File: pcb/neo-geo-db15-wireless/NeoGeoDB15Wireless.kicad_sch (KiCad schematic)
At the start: 3 parts, among them J1 DB15_Female_MountingHoles, U1 RP2040-Zero, U2 NRF24L01_Breakout

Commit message: PCB schematic
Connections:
- net GND: now reaches U1.23 (GND), U2.1 (GND)
- net GND: now also J1.1
- net at U1.20 (GP29): no longer U2.3 (CE)
- net CS: now reaches U2.4 (~{CSN})
- net CS: now also U1.14 (GP13)
- net SCK: now reaches U2.5 (SCK)
- net SCK: now also U1.15 (GP14)
- net MOSI: now reaches U2.6 (MOSI)
- net MOSI: now also U1.16 (GP15)
- net MISO: now reaches U2.7 (MISO)
- net MISO: now also U1.13 (GP12)
- net at U1.19 (GP28): no longer U2.8 (IRQ)
- net DU: now reaches U1.1 (GP0)
- net DU: now also J1.15 (P15)
- net SEL: now reaches U1.10 (GP9)
- net SEL: now also J1.3
- net CE: now reaches U1.17 (GP26)
- net CE: now also U2.3 (CE)
- net IRQ: now reaches U1.18 (GP27)
- net IRQ: now also U2.8 (IRQ)
- net DD: now reaches U1.2 (GP1)
- net DD: now also J1.7
- net VCC: now reaches U1.22 (5V)
- net VCC: now also J1.8
- net DL: now reaches U1.3 (GP2)
- net DL: now also J1.14 (P14)
- net DR: now reaches U1.4 (GP3)
- net DR: now also J1.6
- net BA: now reaches U1.5 (GP4)
- net BA: now also J1.13 (P13)
- net BB: now reaches U1.6 (GP5)
- net BB: now also J1.5
- net BC: now reaches U1.7 (GP6)
- net BC: now also J1.12 (P12)
- net BD: now reaches U1.8 (GP7)
- net BD: now also J1.4
- net STA: now reaches U1.9 (GP8)
- net STA: now also J1.11 (P111)
- no-connect marks 0 -> 8
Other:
- moved on the sheet: J1
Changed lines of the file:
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@@
 (kicad_sch (version 20211123) (generator eeschema)
   (paper "A4")
-  (wire (pts (xy 115.57 92.71) (xy 115.57 83.82))
-    (stroke (width 0) (type default) (color 0 0 0 0))
-  )
-  (wire (pts (xy 153.67 76.2) (xy 130.81 58.42))
-    (stroke (width 0) (type default) (color 0 0 0 0))
-  )
-  (wire (pts (xy 166.37 83.82) (xy 166.37 92.71))
-    (stroke (width 0) (type default) (color 0 0 0 0))
-  )
-  (wire (pts (xy 153.67 73.66) (xy 130.81 55.88))
-    (stroke (width 0) (type default) (color 0 0 0 0))
-  )
+  (no_connect (at 130.81 76.2))
+  (no_connect (at 130.81 78.74))
+  (no_connect (at 130.81 55.88))
+  (no_connect (at 130.81 58.42))
+  (no_connect (at 152.4 24.13))
+  (no_connect (at 149.86 24.13))
+  (no_connect (at 154.94 24.13))
+  (no_connect (at 116.84 31.75))
   (wire (pts (xy 116.84 49.53) (xy 166.37 49.53))
     (stroke (width 0) (type default) (color 0 0 0 0))
@@
     (stroke (width 0) (type default) (color 0 0 0 0))
   )
-  (wire (pts (xy 166.37 92.71) (xy 115.57 92.71))
-    (stroke (width 0) (type default) (color 0 0 0 0))
+  (label "BD" (at 142.24 24.13 90)
+    (effects (font (size 1.27 1.27)) (justify left bottom))
+  )
+  (label "DR" (at 132.08 24.13 90)
+    (effects (font (size 1.27 1.27)) (justify left bottom))
+  )
+  (label "CS" (at 130.81 71.12 0)
+    (effects (font (size 1.27 1.27)) (justify left bottom))
+  )
+  (label "GND" (at 115.57 83.82 270)
+    (effects (font (size 1.27 1.27)) (justify right bottom))
+  )
+  (label "BC" (at 139.7 24.13 90)
+    (effects (font (size 1.27 1.27)) (justify left bottom))
+  )
+  (label "BB" (at 101.6 68.58 180)
+    (effects (font (size 1.27 1.27)) (justify right bottom))
+  )
+  (label "BD" (at 101.6 73.66 180)
+    (effects (font (size 1.27 1.27)) (justify right bottom))
+  )
+  (label "VCC" (at 121.92 24.13 90)
+    (effects (font (size 1.27 1.27)) (justify left bottom))
+  )
+  (label "SCK" (at 130.81 68.58 0)
+    (effects (font (size 1.27 1.27)) (justify left bottom))
+  )
+  (label "IRQ" (at 153.67 76.2 180)
+    (effects (font (size 1.27 1.27)) (justify right bottom))
+  )
+  (label "VCC" (at 114.3 49.53 90)
+    (effects (font (size 1.27 1.27)) (justify left bottom))
+  )
+  (label "DU" (at 101.6 55.88 180)
+    (effects (font (size 1.27 1.27)) (justify right bottom))
+  )
+  (label "DR" (at 101.6 63.5 180)
+    (effects (font (size 1.27 1.27)) (justify right bottom))
+  )
+  (label "CE" (at 153.67 73.66 180)
+    (effects (font (size 1.27 1.27)) (justify right bottom))
+  )
+  (label "STA" (at 101.6 76.2 180)
+    (effects (font (size 1.27 1.27)) (justify right bottom))
+  )
+  (label "DD" (at 127 24.13 90)
+    (effects (font (size 1.27 1.27)) (justify left bottom))
+  )
+  (label "MISO" (at 130.81 73.66 0)
+    (effects (font (size 1.27 1.27)) (justify left bottom))
+  )
+  (label "CE" (at 130.81 63.5 0)
+    (effects (font (size 1.27 1.27)) (justify left bottom))
+  )
+  (label "CS" (at 153.67 68.58 180)
+    (effects (font (size 1.27 1.27)) (justify right bottom))
+  )
+  (label "GND" (at 157.48 24.13 90)
+    (effects (font (size 1.27 1.27)) (justify left bottom))
+  )
+  (label "BC" (at 101.6 71.12 180)
+    (effects (font (size 1.27 1.27)) (justify right bottom))
+  )
+  (label "BA" (at 101.6 66.04 180)
+    (effects (font (size 1.27 1.27)) (justify right bottom))
+  )
+  (label "SCK" (at 153.67 66.04 180)
+    (effects (font (size 1.27 1.27)) (justify right bottom))
+  )
+  (label "BB" (at 137.16 24.13 90)
+    (effects (font (size 1.27 1.27)) (justify left bottom))
+  )
+  (label "MOSI" (at 130.81 66.04 0)
+    (effects (font (size 1.27 1.27)) (justify left bottom))
+  )
+  (label "MISO" (at 153.67 63.5 180)
+    (effects (font (size 1.27 1.27)) (justify right bottom))
+  )
+  (label "BA" (at 134.62 24.13 90)
+    (effects (font (size 1.27 1.27)) (justify left bottom))
+  )
+  (label "DU" (at 124.46 24.13 90)
+    (effects (font (size 1.27 1.27)) (justify left bottom))
+  )
+  (label "STA" (at 144.78 24.13 90)
+    (effects (font (size 1.27 1.27)) (justify left bottom))
+  )
+  (label "DD" (at 101.6 58.42 180)
+    (effects (font (size 1.27 1.27)) (justify right bottom))
+  )
+  (label "MOSI" (at 153.67 60.96 180)
+    (effects (font (size 1.27 1.27)) (justify right bottom))
+  )
+  (label "DL" (at 101.6 60.96 180)
+    (effects (font (size 1.27 1.27)) (justify right bottom))
+  )
+  (label "SEL" (at 101.6 78.74 180)
+    (effects (font (size 1.27 1.27)) (justify right bottom))
+  )
+  (label "DL" (at 129.54 24.13 90)
+    (effects (font (size 1.27 1.27)) (justify left bottom))
+  )
+  (label "IRQ" (at 130.81 60.96 0)
+    (effects (font (size 1.27 1.27)) (justify left bottom))
+  )
+  (label "GND" (at 166.37 83.82 270)
+    (effects (font (size 1.27 1.27)) (justify right bottom))
+  )
+  (label "SEL" (at 147.32 24.13 90)
+    (effects (font (size 1.27 1.27)) (justify left bottom))
   )
   (symbol (lib_id "RF:NRF24L01_Breakout") (at 166.37 68.58 0) (unit 1)
@@
     (pin "9")
   )
-  (symbol (lib_id "Connector:DB15_Female_MountingHoles") (at 139.7 31.75 90) (unit 1)
+  (symbol (lib_id "Connector:DB15_Female_MountingHoles") (at 139.7 31.75 270) (unit 1)
     (in_bom yes) (on_board yes) (fields_autoplaced)
-    (property "Reference" "J1" (id 0) (at 139.7 22.86 90))
-    (property "Value" "DB15_Female_MountingHoles" (id 1) (at 139.7 25.4 90))
+    (property "Reference" "J1" (id 0) (at 139.7 38.1 90))
+    (property "Value" "DB15_Female_MountingHoles" (id 1) (at 139.7 40.64 90))
     (property "Footprint" "DB15:TE_Connectivity-5747845-5-0-0-MFG" (id 2) (at 139.7 31.75 0)
       (effects (font (size 1.27 1.27)) hide)

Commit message: Making the right size
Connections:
- net 3V3: now reaches U1.21 (3V3), U2.2 (VCC)
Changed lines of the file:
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@@
   (no_connect (at 154.94 24.13))
   (no_connect (at 116.84 31.75))
-  (wire (pts (xy 116.84 49.53) (xy 166.37 49.53))
-    (stroke (width 0) (type default) (color 0 0 0 0))
-  )
-  (wire (pts (xy 166.37 49.53) (xy 166.37 53.34))
-    (stroke (width 0) (type default) (color 0 0 0 0))
-  )
   (label "BD" (at 142.24 24.13 90)
     (effects (font (size 1.27 1.27)) (justify left bottom))
@@
   )
   (label "BC" (at 139.7 24.13 90)
+    (effects (font (size 1.27 1.27)) (justify left bottom))
+  )
+  (label "3V3" (at 116.84 49.53 90)
     (effects (font (size 1.27 1.27)) (justify left bottom))
   )
@@
     (effects (font (size 1.27 1.27)) (justify right bottom))
   )
+  (label "3V3" (at 166.37 53.34 90)
+    (effects (font (size 1.27 1.27)) (justify left bottom))
+  )
   (label "VCC" (at 114.3 49.53 90)

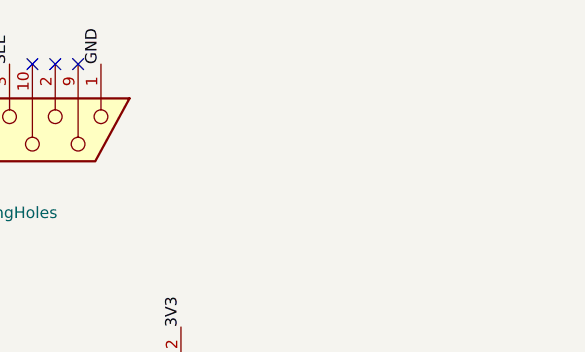
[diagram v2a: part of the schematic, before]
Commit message: Adds decoupling caps
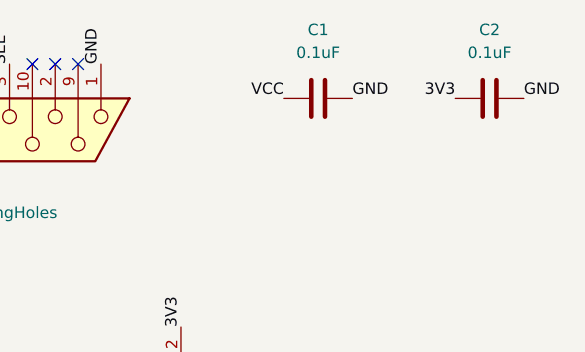
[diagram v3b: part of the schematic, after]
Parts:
- added C1, C2: 0.1uF, Capacitor_SMD:C_0603_1608Metric_Pad1.08x0.95mm_HandSolder, symbol Device:C
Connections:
- net 3V3: now also C2.1
- net GND: now also C1.2, C2.2
- net VCC: now also C1.1
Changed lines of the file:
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@@
     (effects (font (size 1.27 1.27)) (justify left bottom))
+  )
+  (label "3V3" (at 196.85 27.94 180)
+    (effects (font (size 1.27 1.27)) (justify right bottom))
   )
   (label "MISO" (at 130.81 73.66 0)
@@
     (effects (font (size 1.27 1.27)) (justify right bottom))
   )
+  (label "VCC" (at 177.8 27.94 180)
+    (effects (font (size 1.27 1.27)) (justify right bottom))
+  )
   (label "BA" (at 134.62 24.13 90)
     (effects (font (size 1.27 1.27)) (justify left bottom))
@@
     (effects (font (size 1.27 1.27)) (justify left bottom))
   )
+  (label "GND" (at 204.47 27.94 0)
+    (effects (font (size 1.27 1.27)) (justify left bottom))
+  )
   (label "STA" (at 144.78 24.13 90)
+    (effects (font (size 1.27 1.27)) (justify left bottom))
+  )
+  (label "GND" (at 185.42 27.94 0)
     (effects (font (size 1.27 1.27)) (justify left bottom))
   )
@@
     (pin "7")
     (pin "8")
+  )
+  (symbol (lib_id "Device:C") (at 181.61 27.94 90) (unit 1)
+    (in_bom yes) (on_board yes) (fields_autoplaced)
+    (property "Reference" "C1" (id 0) (at 181.61 20.32 90))
+    (property "Value" "0.1uF" (id 1) (at 181.61 22.86 90))
+    (property "Footprint" "Capacitor_SMD:C_0603_1608Metric_Pad1.08x0.95mm_HandSolder" (id 2) (at 185.42 26.9748 0)
+      (effects (font (size 1.27 1.27)) hide)
+    )
+    (property "Datasheet" "~" (id 3) (at 181.61 27.94 0)
+      (effects (font (size 1.27 1.27)) hide)
+    )
+    (pin "1")
+    (pin "2")
   )
   (symbol (lib_id "RP2040Zero:RP2040-Zero") (at 115.57 66.04 0) (unit 1)
@@
     (pin "9")
   )
+  (symbol (lib_id "Device:C") (at 200.66 27.94 90) (unit 1)
+    (in_bom yes) (on_board yes) (fields_autoplaced)
+    (property "Reference" "C2" (id 0) (at 200.66 20.32 90))
+    (property "Value" "0.1uF" (id 1) (at 200.66 22.86 90))
+    (property "Footprint" "Capacitor_SMD:C_0603_1608Metric_Pad1.08x0.95mm_HandSolder" (id 2) (at 204.47 26.9748 0)
+      (effects (font (size 1.27 1.27)) hide)
+    )
+    (property "Datasheet" "~" (id 3) (at 200.66 27.94 0)
+      (effects (font (size 1.27 1.27)) hide)
+    )
+    (pin "1")
+    (pin "2")
+  )
   (sheet_instances
     (path "/" (page "1"))
   )
   (symbol_instances
+    (path "/5600fa70-7237-419a-a1e7-e59e3f85f285"
+      (reference "C1") (unit 1) (value "0.1uF") (footprint "Capacitor_SMD:C_0603_1608Metric_Pad1.08x0.95mm_HandSolder")
+    )
+    (path "/efed16f8-8695-4c2e-90ae-063653f0ab84"
+      (reference "C2") (unit 1) (value "0.1uF") (footprint "Capacitor_SMD:C_0603_1608Metric_Pad1.08x0.95mm_HandSolder")
+    )
     (path "/dad04a51-3cbf-4f9b-b9b9-52635f5ef12c"
       (reference "J1") (unit 1) (value "DB15_Female_MountingHoles") (footprint "DB15:TE_Connectivity-5747845-5-0-0-MFG")

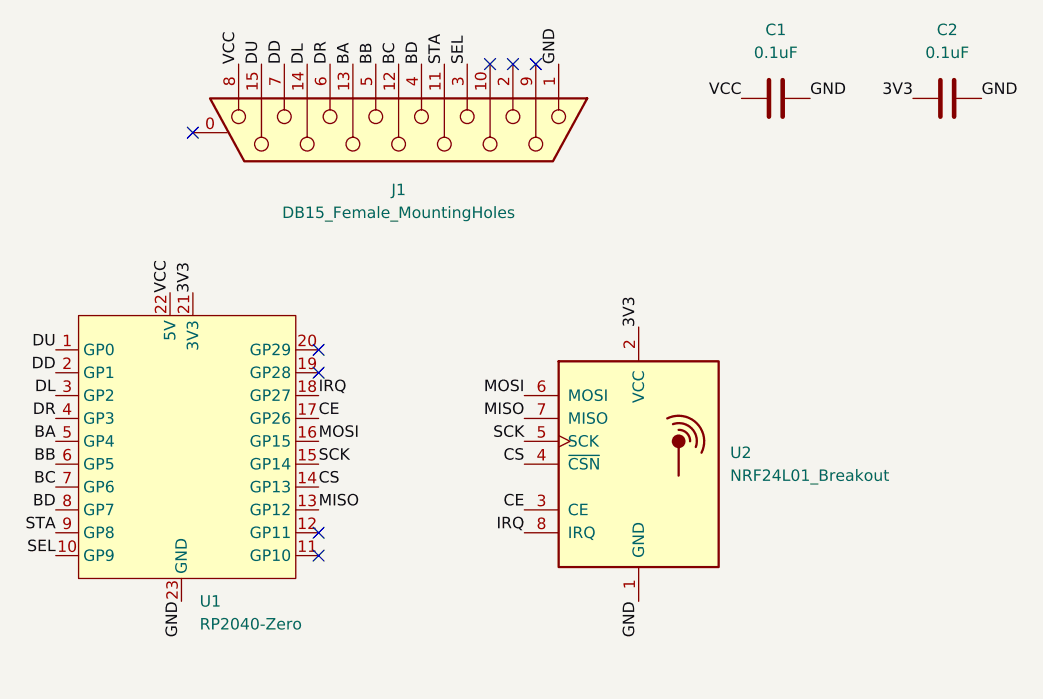
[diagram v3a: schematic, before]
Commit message: Fixes errors in PCB, incorrect pin numbering on RP2040, unconnected grounds, ground mounting points, some vias to increase ground plane flood
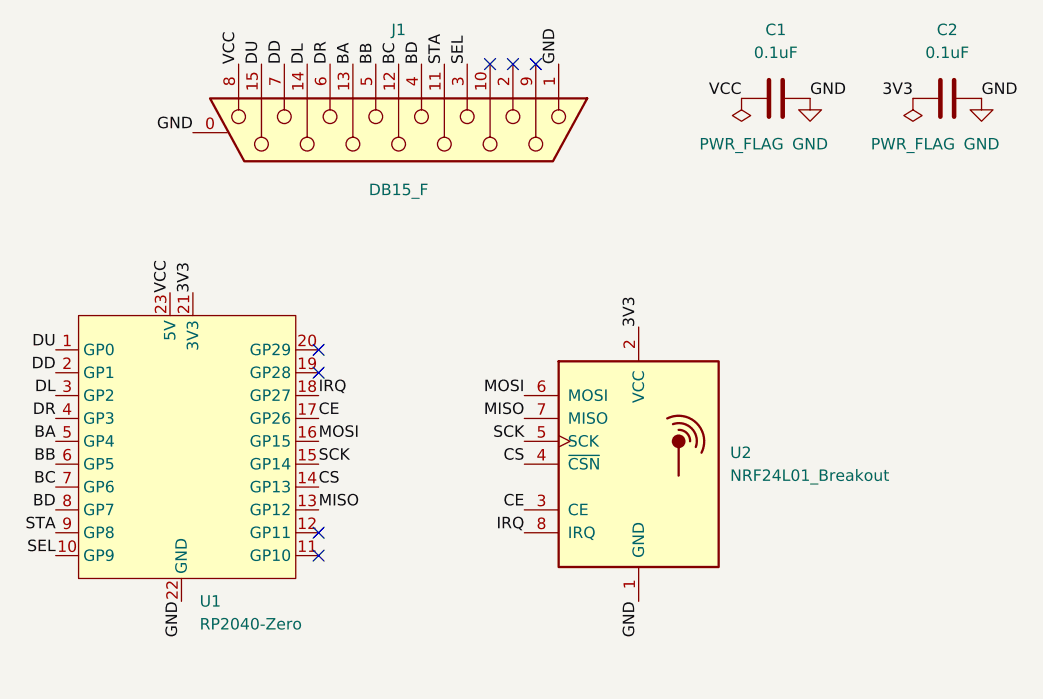
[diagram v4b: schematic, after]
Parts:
- J1: value DB15_Female_MountingHoles -> DB15_F; symbol Connector:DB15_Female_MountingHoles -> Connector:DA15_Receptacle_MountingHoles
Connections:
- net GND: now also J1.0 (PAD), U1.22 (GND); no longer U1.23 (GND)
- net VCC: now also U1.23 (5V); no longer U1.22 (5V)
- no-connect marks 8 -> 7
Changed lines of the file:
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@@
   (no_connect (at 149.86 24.13))
   (no_connect (at 154.94 24.13))
-  (no_connect (at 116.84 31.75))
   (label "BD" (at 142.24 24.13 90)
     (effects (font (size 1.27 1.27)) (justify left bottom))
@@
   (label "GND" (at 185.42 27.94 0)
     (effects (font (size 1.27 1.27)) (justify left bottom))
+  )
+  (label "GND" (at 116.84 31.75 180)
+    (effects (font (size 1.27 1.27)) (justify right bottom))
   )
   (label "DD" (at 101.6 58.42 180)
@@
     (pin "9")
   )
-  (symbol (lib_id "Connector:DB15_Female_MountingHoles") (at 139.7 31.75 270) (unit 1)
-    (in_bom yes) (on_board yes) (fields_autoplaced)
-    (property "Reference" "J1" (id 0) (at 139.7 38.1 90))
-    (property "Value" "DB15_Female_MountingHoles" (id 1) (at 139.7 40.64 90))
+  (symbol (lib_id "power:PWR_FLAG") (at 196.85 27.94 180) (unit 1)
+    (in_bom yes) (on_board yes) (fields_autoplaced)
+    (property "Reference" "#FLG0103" (id 0) (at 196.85 29.845 0)
+      (effects (font (size 1.27 1.27)) hide)
+    )
+    (property "Value" "PWR_FLAG" (id 1) (at 196.85 33.02 0))
+    (property "Footprint" "" (id 2) (at 196.85 27.94 0)
+      (effects (font (size 1.27 1.27)) hide)
+    )
+    (property "Datasheet" "~" (id 3) (at 196.85 27.94 0)
+      (effects (font (size 1.27 1.27)) hide)
+    )
+    (pin "1")
+  )
+  (symbol (lib_id "power:PWR_FLAG") (at 177.8 27.94 180) (unit 1)
+    (in_bom yes) (on_board yes) (fields_autoplaced)
+    (property "Reference" "#FLG0101" (id 0) (at 177.8 29.845 0)
+      (effects (font (size 1.27 1.27)) hide)
+    )
+    (property "Value" "PWR_FLAG" (id 1) (at 177.8 33.02 0))
+    (property "Footprint" "" (id 2) (at 177.8 27.94 0)
+      (effects (font (size 1.27 1.27)) hide)
+    )
+    (property "Datasheet" "~" (id 3) (at 177.8 27.94 0)
+      (effects (font (size 1.27 1.27)) hide)
+    )
+    (pin "1")
+  )
+  (symbol (lib_id "power:GND") (at 185.42 27.94 0) (unit 1)
+    (in_bom yes) (on_board yes) (fields_autoplaced)
+    (property "Reference" "#PWR0102" (id 0) (at 185.42 34.29 0)
+      (effects (font (size 1.27 1.27)) hide)
+    )
+    (property "Value" "GND" (id 1) (at 185.42 33.02 0))
+    (property "Footprint" "" (id 2) (at 185.42 27.94 0)
+      (effects (font (size 1.27 1.27)) hide)
+    )
+    (property "Datasheet" "" (id 3) (at 185.42 27.94 0)
+      (effects (font (size 1.27 1.27)) hide)
+    )
+    (pin "1")
+  )
+  (symbol (lib_id "power:GND") (at 204.47 27.94 0) (unit 1)
+    (in_bom yes) (on_board yes) (fields_autoplaced)
+    (property "Reference" "#PWR0101" (id 0) (at 204.47 34.29 0)
+      (effects (font (size 1.27 1.27)) hide)
+    )
+    (property "Value" "GND" (id 1) (at 204.47 33.02 0))
+    (property "Footprint" "" (id 2) (at 204.47 27.94 0)
+      (effects (font (size 1.27 1.27)) hide)
+    )
+    (property "Datasheet" "" (id 3) (at 204.47 27.94 0)
+      (effects (font (size 1.27 1.27)) hide)
+    )
+    (pin "1")
+  )
+  (symbol (lib_id "Connector:DA15_Receptacle_MountingHoles") (at 139.7 31.75 270) (unit 1)
+    (in_bom yes) (on_board yes)
+    (property "Reference" "J1" (id 0) (at 139.7 20.32 90))
+    (property "Value" "DB15_F" (id 1) (at 139.7 38.1 90))
     (property "Footprint" "DB15:TE_Connectivity-5747845-5-0-0-MFG" (id 2) (at 139.7 31.75 0)
       (effects (font (size 1.27 1.27)) hide)
@@
   )
   (symbol_instances
+    (path "/bda6dd11-eb99-403c-9af9-fb9da2050c17"
+      (reference "#FLG0101") (unit 1) (value "PWR_FLAG") (footprint "")
+    )
+    (path "/a70928a0-612a-4641-bfb0-31e445ae085a"
+      (reference "#FLG0103") (unit 1) (value "PWR_FLAG") (footprint "")
+    )
+    (path "/c674200a-4e8f-49df-8b20-e3dab3abec4f"
+      (reference "#PWR0101") (unit 1) (value "GND") (footprint "")
+    )
+    (path "/c529e3e4-71ad-472c-aa0d-e5b10611fd5d"
+      (reference "#PWR0102") (unit 1) (value "GND") (footprint "")
+    )
     (path "/5600fa70-7237-419a-a1e7-e59e3f85f285"
       (reference "C1") (unit 1) (value "0.1uF") (footprint "Capacitor_SMD:C_0603_1608Metric_Pad1.08x0.95mm_HandSolder")
@@
     )
     (path "/dad04a51-3cbf-4f9b-b9b9-52635f5ef12c"
-      (reference "J1") (unit 1) (value "DB15_Female_MountingHoles") (footprint "DB15:TE_Connectivity-5747845-5-0-0-MFG")
+      (reference "J1") (unit 1) (value "DB15_F") (footprint "DB15:TE_Connectivity-5747845-5-0-0-MFG")
     )
     (path "/5b168a7b-7078-4351-82a8-b1d62bb6fd1f"
